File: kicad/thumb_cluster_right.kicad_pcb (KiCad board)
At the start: 2 copper layers, 41.2 x 43.8 mm, 16 parts, among them J1 Conn_01x07

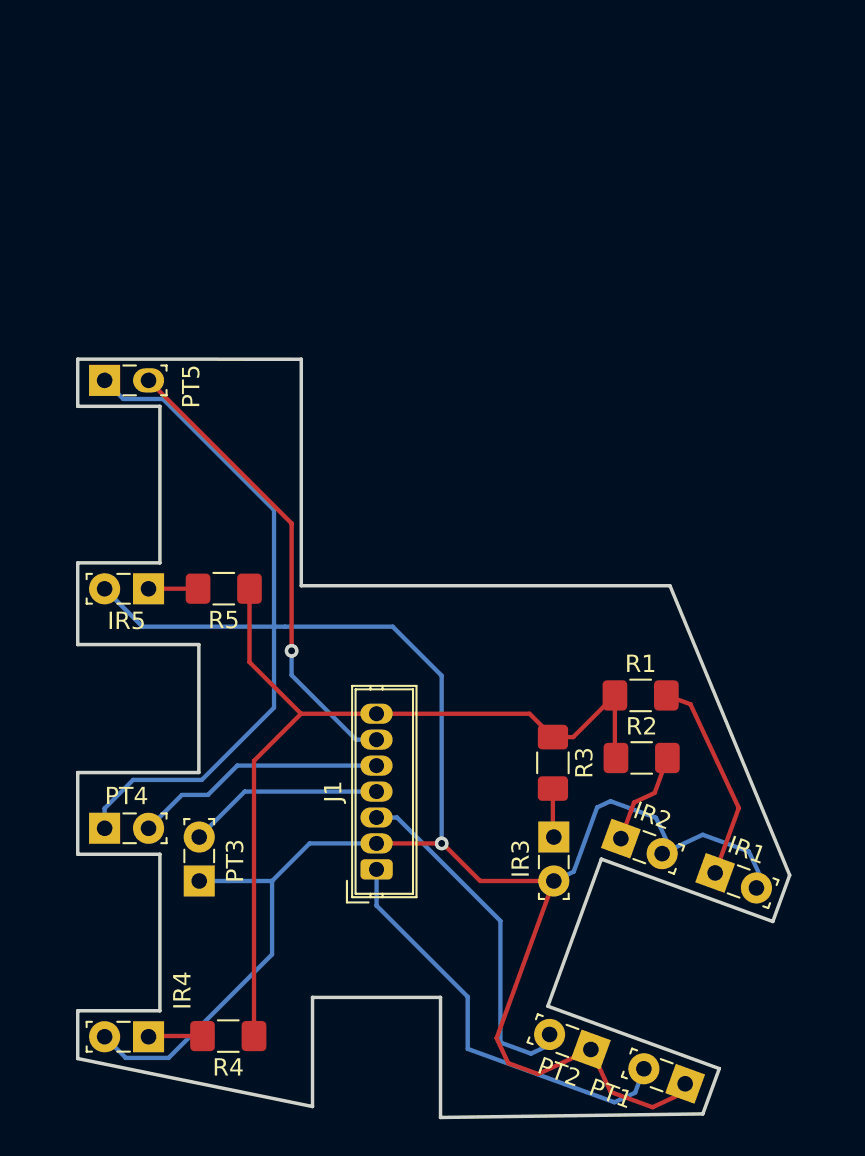
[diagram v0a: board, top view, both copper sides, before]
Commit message: Add a nub indicating the lens on the IR and PT footprints
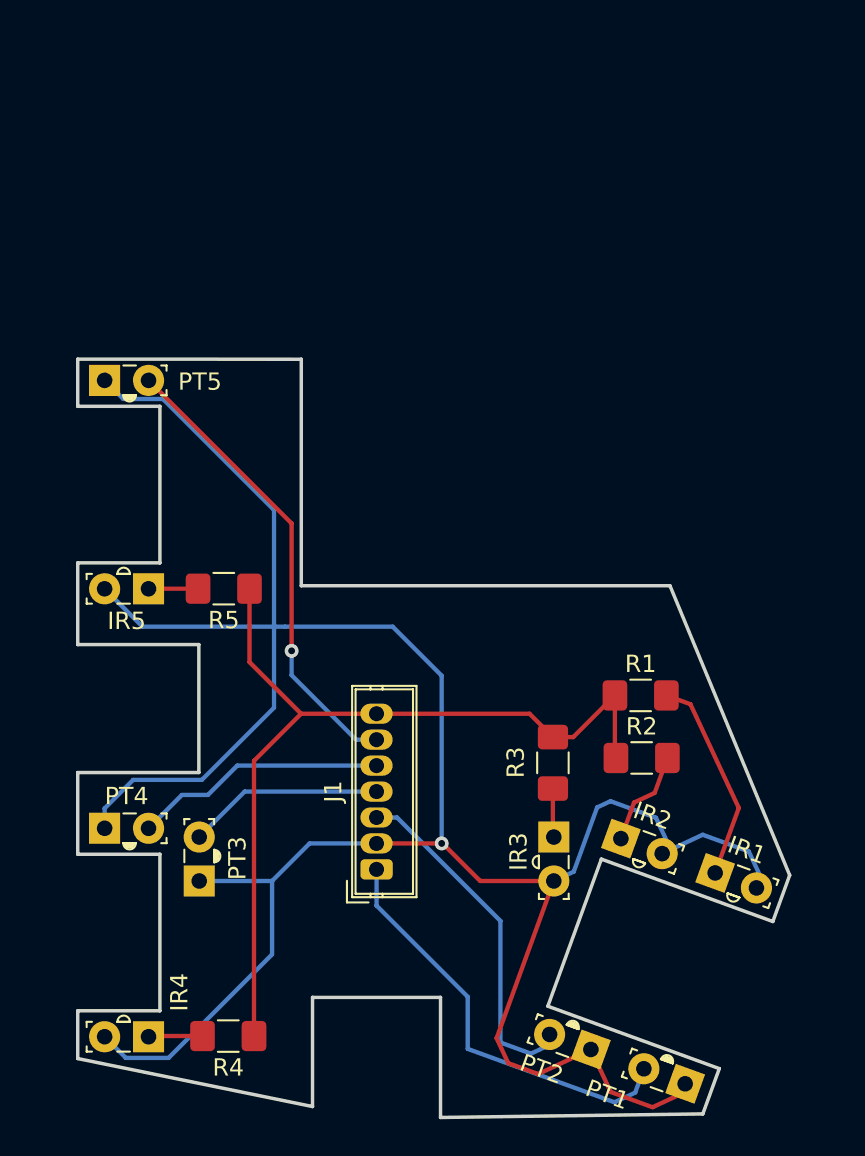
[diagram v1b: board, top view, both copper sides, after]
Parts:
- IR1, IR2, IR3, IR4, IR5: footprint LED_THT:LED_SideEmitter_Rectangular_W4.5mm_H1.6mm -> lalboard:IR908-7C-F
- PT1, PT2, PT3, PT4, PT5: footprint LED_THT:LED_SideEmitter_Rectangular_W4.5mm_H1.6mm -> lalboard:PT908-7C-F

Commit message: Update the design of the right thumb cluster pcb
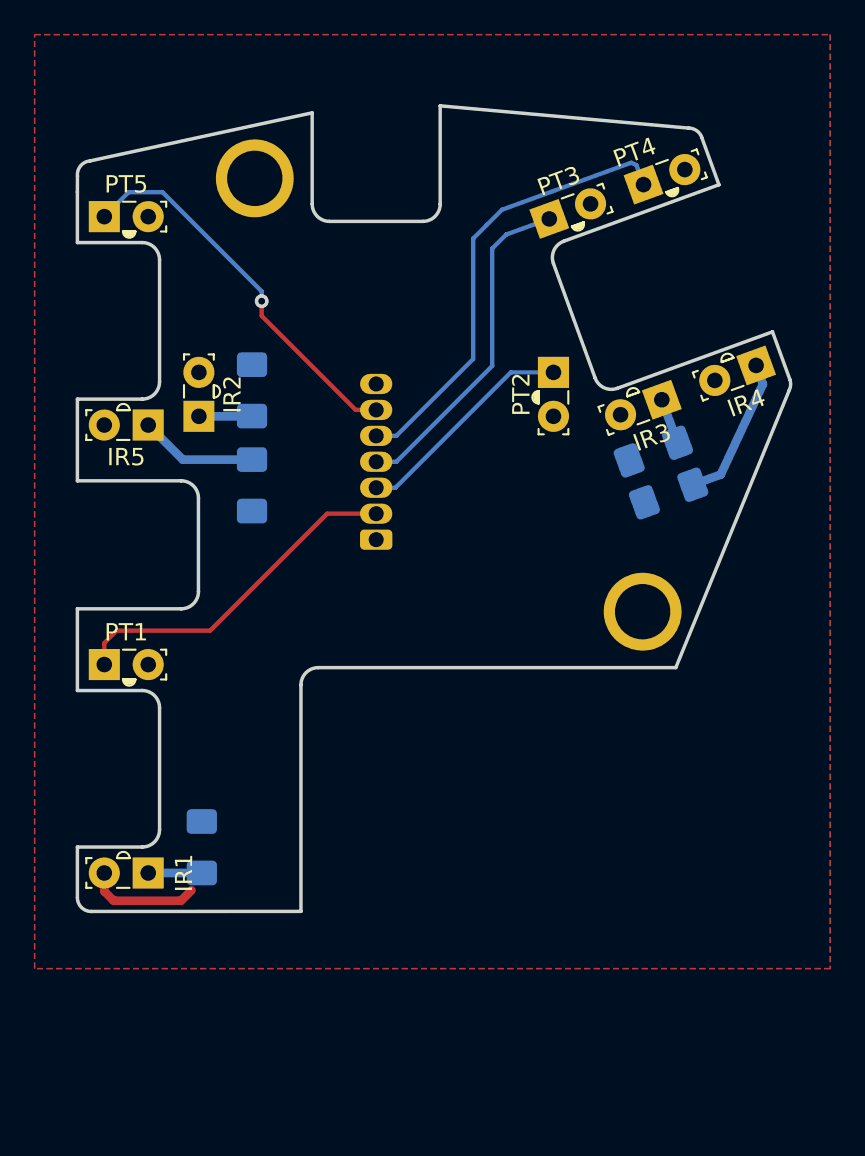
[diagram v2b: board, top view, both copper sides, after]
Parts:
- added ?: , , F.Cu at (144.4, 97.6)
- added ?: , , F.Cu at (135.1, 93.6)
- added REF**: MountingHole_3.2mm_M3_Pad, MountingHole:MountingHole_3.2mm_M3_Pad, F.Cu at (135.7, 66.3)
- added REF**: MountingHole_3.2mm_M3_Pad, MountingHole:MountingHole_3.2mm_M3_Pad, F.Cu at (158.2, 91.4)
- J1, R2, R3, R4, R5: moved to B.Cu
- R1: value 150 -> 100; moved to B.Cu
- moved IR4 52.3 mm to (164.7, 77.1), turned to 200 degrees
- moved PT4 48.5 mm to (158.2, 66.7), turned to 20 degrees
- moved PT3 43.3 mm to (152.8, 68.7), turned to 20 degrees
- moved PT1 41.4 mm to (127.0, 94.4), turned to 0 degrees
- moved R4 40.4 mm to (159.7, 84.5), turned to 20 degrees
- moved PT2 39.2 mm to (153.0, 77.5), turned to 270 degrees
- moved IR2 34.5 mm to (132.5, 80.1), turned to 90 degrees
- moved IR1 32.8 mm to (129.6, 106.5), turned to 180 degrees
- moved R2 31.0 mm to (135.6, 78.6), turned to 270 degrees
- moved R1 26.8 mm to (132.7, 105.0), turned to 270 degrees
- moved IR3 26.0 mm to (159.3, 79.1), turned to 200 degrees
- moved J1 19.1 mm to (142.8, 87.2)
- moved R3 18.9 mm to (158.8, 82.1), turned to 20 degrees
- moved PT5 9.47 mm to (127.0, 68.5)
- moved IR5 9.47 mm to (129.6, 80.6)
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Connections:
- J1 pad 1: C1 -> +5V
- J1 pad 2: +5V -> C1
- J1 pad 3: C3 -> C2
- J1 pad 4: C4 -> C3
- J1 pad 5: C5 -> C4
- J1 pad 6: C6 -> C5
- PT1 pad 1: +5V -> C1
- PT1 pad 2: C1 -> +5V
- PT2 pad 1: +5V -> C2
- PT2 pad 2: C3 -> +5V
- PT3 pad 1: +5V -> C3
- PT3 pad 2: C4 -> +5V
- PT4 pad 1: +5V -> C4
- PT4 pad 2: C5 -> +5V
- PT5 pad 1: +5V -> C5
- PT5 pad 2: C6 -> +5V
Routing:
- net +5V: track 151.2 -> 6.57 mm, vias 1 -> 0
- net GND: track 51.8 -> 0.00 mm
- net C6: track 26.9 -> 0.00 mm, vias 1 -> 0
- net C4: track 11.3 -> 26.3 mm
- net C2: track 0.00 -> 13.0 mm
- net Net-(IR1-Pad1): track 12.1 -> 2.68 mm
- net C5: track 14.7 -> 22.4 mm, vias 0 -> 1
- net Net-(IR4-Pad1): track 3.14 -> 8.64 mm
- net C1: track 24.4 -> 20.1 mm
- net Net-(IR5-Pad1): track 3.08 -> 6.83 mm
- net Net-(IR2-Pad1): track 5.79 -> 2.51 mm
- net C3: track 20.2 -> 19.6 mm
- added copper zone on F.Cu, net +5V
- added copper zone on B.Cu, net GND
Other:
- board size 41.2 x 43.8 mm -> 41.2 x 46.6 mm
- net class Power added: clearance 0.2, trace_width 0.5, via_dia 0.8, via_drill 0.4
- board text added: "100"
- board text added: "150"
- board text added: "Max internal corner radius: 1.0mm (for all internal corners)"
- board text added: "lalboard.com right thumb cluster v0.1"

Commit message: Update thumb cluster pcbs to v0.2
This shuffles the switch numbering and order on the connector,
so that the center key is on the same pin of the connector (pin 4)
as the center key of the finger clusters.

These keys on the thumb and finger clusters have inverted logic from
all the other keys, due to the physical design of the switches. This
puts the inverted keys on the same pin/column. This simplifies the
firmware a bit, because it can just assume that pin is always inverted.
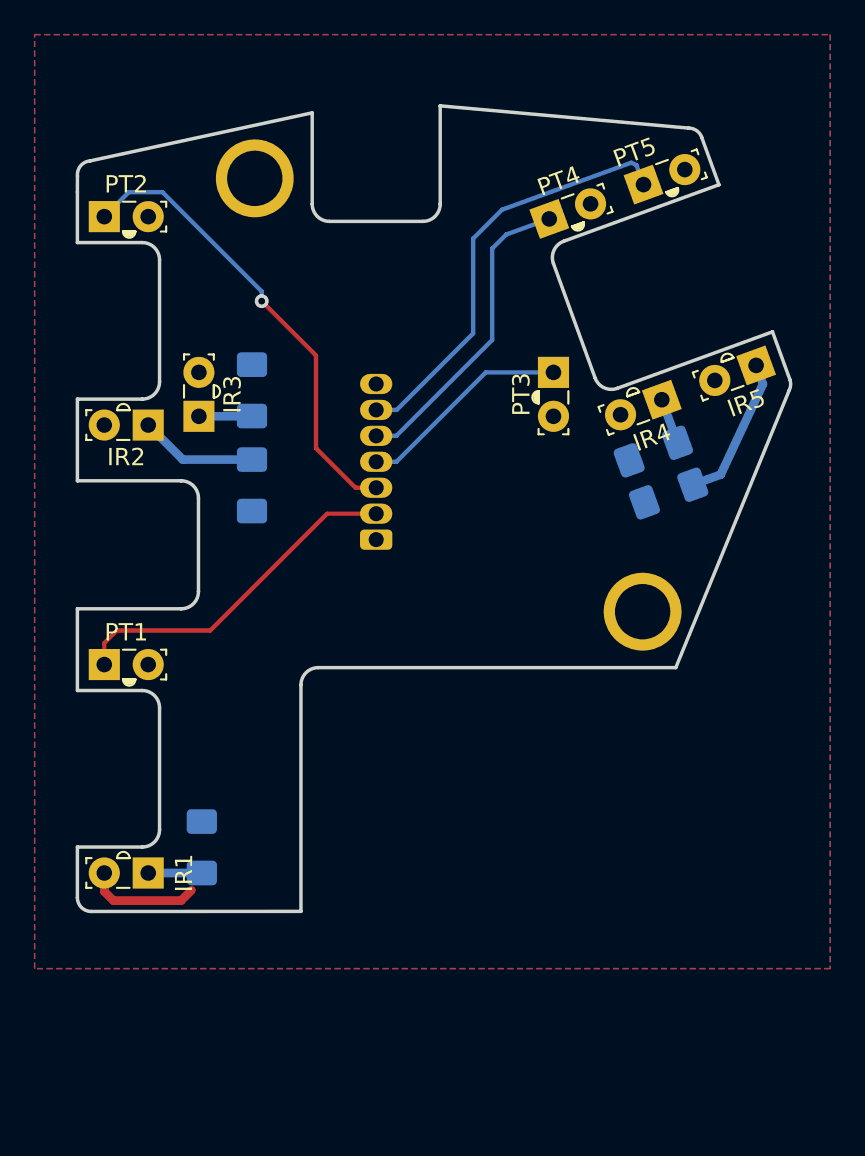
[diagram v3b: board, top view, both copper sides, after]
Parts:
- removed ? (x2): , 
- removed the R5 at (135.6, 84.1)
- removed REF** (x2): MountingHole_3.2mm_M3_Pad, MountingHole:MountingHole_3.2mm_M3_Pad
- added H1: MountingHole_Pad, MountingHole:MountingHole_3.2mm_M3_Pad, F.Cu at (158.2, 91.4)
- added H2: MountingHole_Pad, MountingHole:MountingHole_3.2mm_M3_Pad, F.Cu at (135.7, 66.3)
- added R2: 150, Resistor_SMD:R_1206_3216Metric_Pad1.42x1.75mm_HandSolder, B.Cu at (135.6, 84.1)
- renumbered IR5 to IR2, IR2 to IR3, IR3 to IR4, IR4 to IR5, PT5 to PT2, PT2 to PT3, PT3 to PT4, PT4 to PT5, R2 to R3, R3 to R4, R4 to R5
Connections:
- PT2 pad 1: C5 -> C2
- PT3 pad 1: C2 -> C3
- PT4 pad 1: C3 -> C4
- PT5 pad 1: C4 -> C5
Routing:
- net C2: track 13.0 -> 26.9 mm, vias 0 -> 1
- net C4: track 26.3 -> 18.1 mm
- net C3: track 19.6 -> 12.4 mm
- net C5: track 22.4 -> 24.8 mm, vias 1 -> 0
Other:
- board text added: "lalboard.com right thumb cluster v0.2"
- board text removed: "lalboard.com right thumb cluster v0.1"

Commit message: Update the various sensitivity-related resistor values
This updates the transimpedance amplifier resistors to 2k, and adjusts
the LED drive resistors to an appropriate level, from empirical testing.
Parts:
- R1: value 100 -> 56
- R2: value 150 -> 100
- R3: value 150 -> 120
- R4: value 150 -> 180
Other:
- board text removed: "100"
- board text removed: "150"
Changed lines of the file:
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@@
   (general
     (thickness 1.6)
-    (drawings 123)
+    (drawings 118)
     (tracks 43)
     (zones 0)
@@
       (effects (font (size 1 1) (thickness 0.15)) (justify mirror))
     )
-    (fp_text value 150 (at 0 1.9 90) (layer B.Fab)
+    (fp_text value 100 (at 0 1.8 90) (layer B.SilkS)
       (effects (font (size 1 1) (thickness 0.15)) (justify mirror))
     )
@@
       (effects (font (size 1 1) (thickness 0.15)) (justify mirror))
     )
-    (fp_text value 150 (at -3.893519 0.002918 20) (layer B.Fab)
+    (fp_text value 150 (at -3.893519 0.002918 20) (layer B.SilkS)
       (effects (font (size 1 1) (thickness 0.15)) (justify mirror))
     )
@@
       (effects (font (size 1 1) (thickness 0.15)) (justify mirror))
     )
-    (fp_text value 150 (at -3.893519 -0.016679 20) (layer B.Fab)
+    (fp_text value 180 (at -3.893519 -0.016679 20) (layer B.SilkS)
       (effects (font (size 1 1) (thickness 0.15)) (justify mirror))
     )
@@
       (effects (font (size 1 1) (thickness 0.15)) (justify mirror))
     )
-    (fp_text value 150 (at 0 -1.82 90) (layer B.Fab)
+    (fp_text value 120 (at 0 -1.8 90) (layer B.SilkS)
       (effects (font (size 1 1) (thickness 0.15)) (justify mirror))
     )
@@
       (effects (font (size 1 1) (thickness 0.15)) (justify mirror))
     )
-    (fp_text value 100 (at 0 -1.82 90) (layer B.Fab)
+    (fp_text value 56 (at 0 -1.82 90) (layer B.SilkS)
       (effects (font (size 1 1) (thickness 0.15)) (justify mirror))
     )
@@
     )
   )
-  (gr_text 100 (at 134.515154 104.972918 90) (layer B.SilkS)
-    (effects (font (size 1 1) (thickness 0.15)) (justify mirror))
-  )
-  (gr_text 150 (at 137.415154 78.438996 90) (layer B.SilkS)
-    (effects (font (size 1 1) (thickness 0.15)) (justify mirror))
-  )
-  (gr_text 150 (at 137.415154 83.938996 90) (layer B.SilkS)
-    (effects (font (size 1 1) (thickness 0.15)) (justify mirror))
-  )
   (gr_text "Max internal corner radius: 1.0mm\n(for all internal corners)" (at 143.99835 71.987448) (layer F.Fab)
     (effects (font (size 0.5 0.5) (thickness 0.125)))
   )
-  (gr_text 150 (at 155.998694 85.869043 20) (layer B.SilkS)
-    (effects (font (size 1 1) (thickness 0.15)) (justify mirror))
-  )
-  (gr_text 150 (at 155.109441 83.425842 20) (layer B.SilkS)
-    (effects (font (size 1 1) (thickness 0.15)) (justify mirror))
-  )
   (gr_text "lalboard.com\nright thumb cluster\nv0.2" (at 144.95 73.000001) (layer B.SilkS)

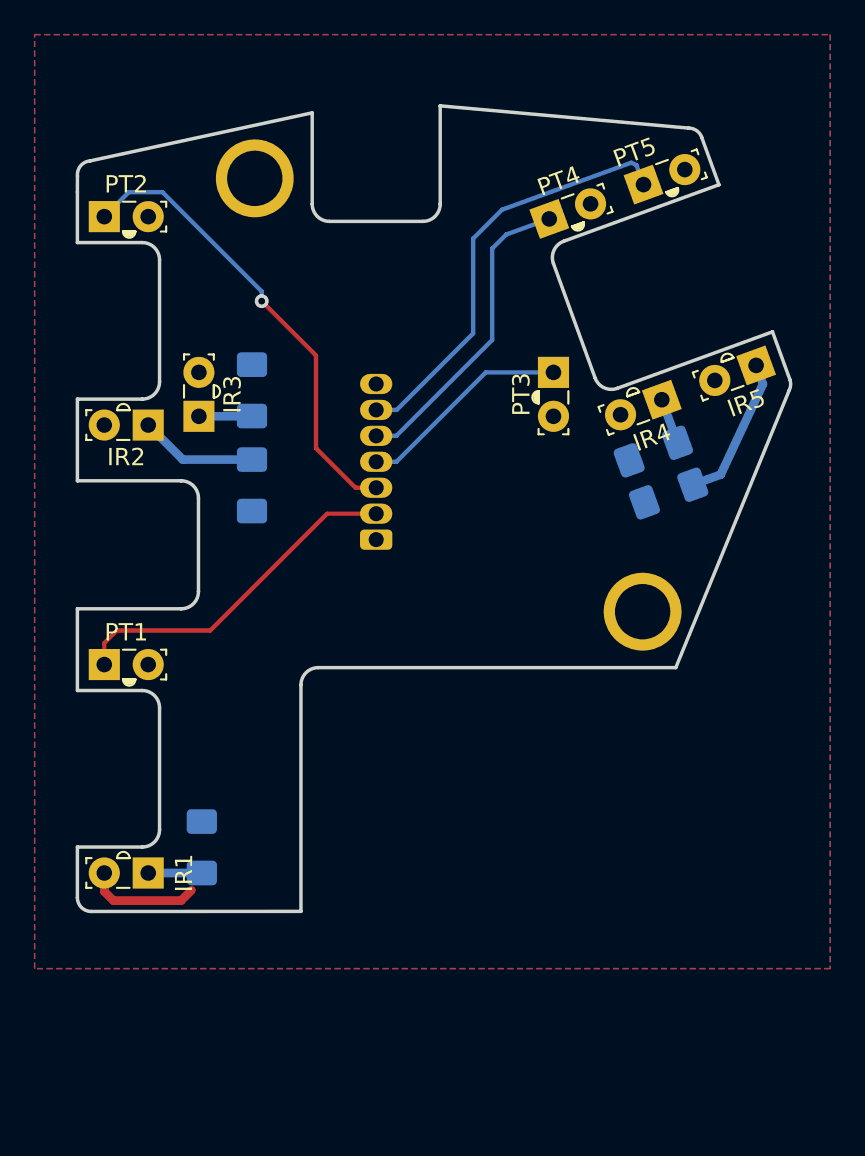
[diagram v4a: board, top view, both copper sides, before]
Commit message: Update thumb clusters to v2.5
Mostly just switching from 1206 to 0805 resistors, and some minor cleanup
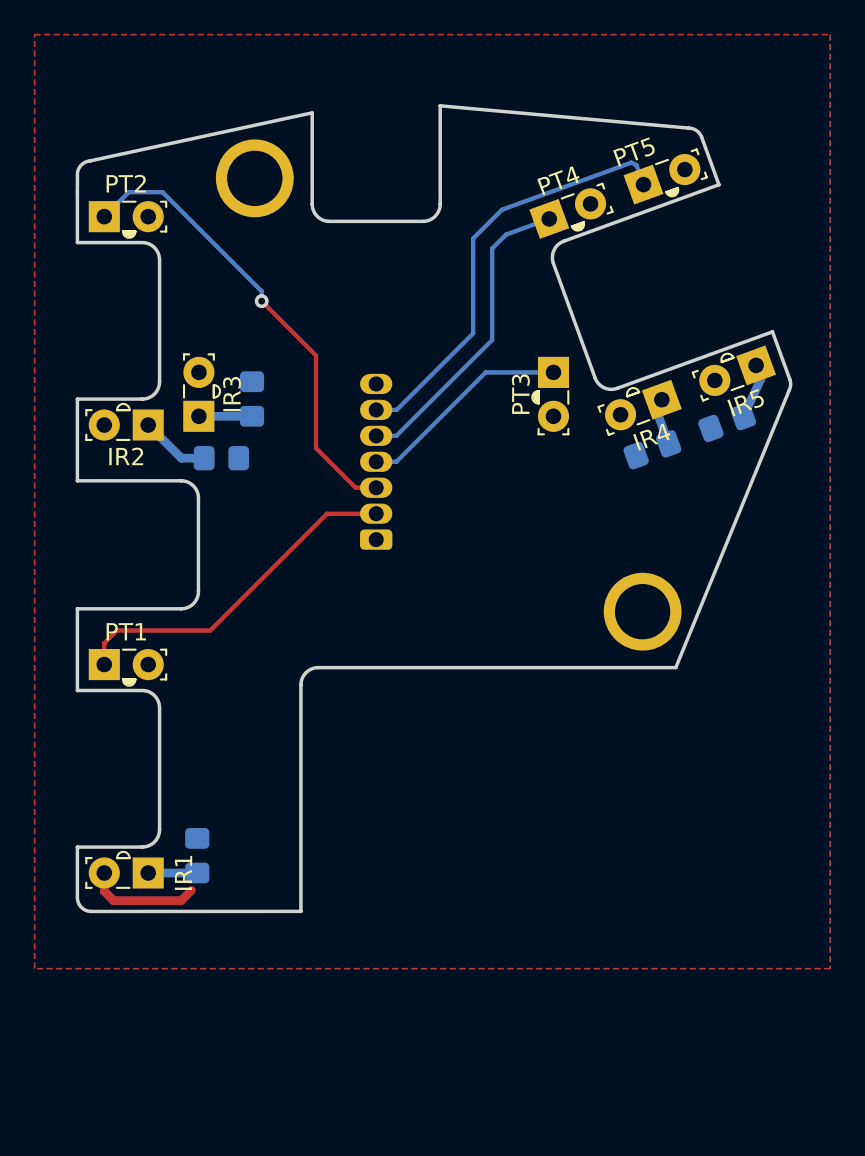
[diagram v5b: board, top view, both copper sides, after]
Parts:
- R1, R2, R3, R4, R5: footprint Resistor_SMD:R_1206_3216Metric_Pad1.42x1.75mm_HandSolder -> Resistor_SMD:R_0805_2012Metric_Pad1.20x1.40mm_HandSolder
- moved R5 5.32 mm to (163.0, 80.4)
- moved R2 2.36 mm to (133.8, 82.5), turned to 180 degrees
- moved R1 0.56 mm to (132.4, 105.5)
- moved R3 0.50 mm to (135.6, 79.1)
- moved R4 0.12 mm to (158.7, 82.0)
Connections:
- net +5V renamed +3.3V
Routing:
- net Net-(IR5-K): track 8.64 -> 3.24 mm
- net Net-(IR2-K): track 6.83 -> 4.03 mm
- net Net-(IR3-K): track 2.51 -> 3.07 mm
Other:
- outline, holes or cut-outs redrawn
- net class Default removed
- net class Power removed
- board text added: "lalboard.com right thumb cluster v2.5"
- board text removed: "Max internal corner radius: 1.0mm (for all internal corners)"
- board text removed: "lalboard.com right thumb cluster v0.2"

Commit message: Delete old lalboard.lib
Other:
- board text added: "lalboard.com right thumb cluster v2.5.0"
- board text removed: "lalboard.com right thumb cluster v2.5"
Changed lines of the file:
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@@
   (gr_line (start 125.475 83.798958) (end 131.475 83.798958)
     (stroke (width 0.2) (type solid)) (layer "Edge.Cuts"))
-  (gr_text "lalboard.com\nright thumb cluster\nv2.5" (at 144.95 73) (layer "B.SilkS")
+  (gr_text "lalboard.com\nright thumb cluster\nv2.5.0" (at 144.95 73) (layer "B.SilkS")
     (effects (font (size 1 1) (thickness 0.15)) (justify mirror))
   )
